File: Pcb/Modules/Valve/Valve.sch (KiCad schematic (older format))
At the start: 19 parts, among them CON1 Valve1, CON2 Valve3, CON3 Power, CON4 Valve2, CON5 Valve4, J1 JACK_RJ45, P1 Servo1, P2 Servo2, Q1 Q_NMOS_GSD, Q2 Q_NMOS_GSD, Q3 Q_NMOS_GSD, Q4 Q_NMOS_GSD

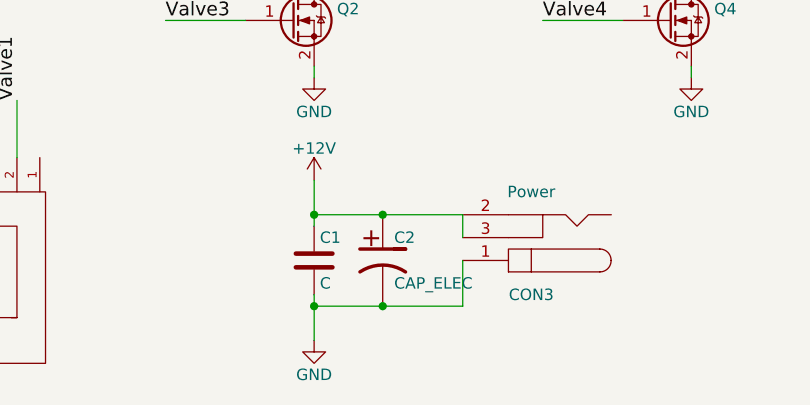
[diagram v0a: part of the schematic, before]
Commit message: Update module pcbs to common format and fix issues.
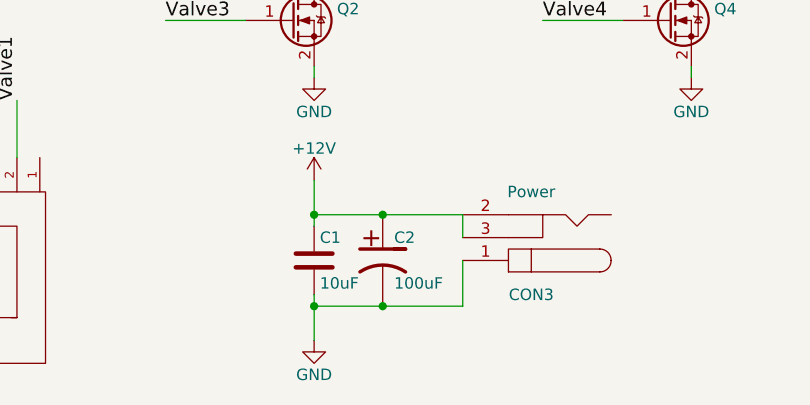
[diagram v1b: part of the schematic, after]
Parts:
- C1: value C -> 10uF
- C2: value CAP_ELEC -> 100uF
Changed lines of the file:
@@
 LIBS:valves
 LIBS:CA6
+LIBS:Valve-cache
 EELAYER 25 0
 EELAYER END
@@
 P 3800 3950
 F 0 "C2" H 3850 4050 50  0000 L CNN
-F 1 "CAP_ELEC" H 3850 3850 50  0000 L CNN
+F 1 "100uF" H 3850 3850 50  0000 L CNN
 F 2 "CA6:c_elec_6.3x5.7" H 3800 3950 60  0001 C CNN
 F 3 "" H 3800 3950 60  0000 C CNN
@@
 P 3500 3950
 F 0 "C1" H 3525 4050 50  0000 L CNN
-F 1 "C" H 3525 3850 50  0000 L CNN
+F 1 "10uF" H 3525 3850 50  0000 L CNN
 F 2 "Capacitors_SMD:C_1206" H 3538 3800 50  0001 C CNN
 F 3 "" H 3500 3950 50  0000 C CNN

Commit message: Update Valve module
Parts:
- added D5: LED, LEDs:LED_0805, symbol LED
- added R1, R3, R5, R7, R9: 1K, Resistors_SMD:R_0603, symbol R
- added R2, R4, R6, R8: 10K, Resistors_SMD:R_0603, symbol R
- added X1, X2, X3, X4: HOLE, Mounting_Holes:MountingHole_2.2mm_M2_ISO14580_Pad, symbol HOLE
- renumbered CON3 to POWER1, Q3 to Q2, Q2 to Q3, CON1 to Valve1, CON4 to Valve2, CON2 to Valve3, CON5 to Valve4
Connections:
- net +12V: now also POWER1.1, Valve1.1, Valve2.1, Valve3.1, Valve4.1, R9.1; no longer POWER1.2, POWER1.3, Valve1.2, Valve1.3, Valve2.2, Valve2.3, Valve3.2, Valve3.3, Valve4.2, Valve4.3
- net GND: now also POWER1.2, D5.1 (K), R2.1, R4.1, R6.1, R8.1; no longer POWER1.1
- net Valve1: now also R1.2; no longer Q1.1 (G)
- net Valve2: now also R3.2; no longer Q2.1 (G)
- net Valve3: now also R5.2; no longer Q3.1 (G)
- net Valve4: now also R7.2; no longer Q4.1 (G)
- net at D1.2 (A), Q1.3 (D): now also Valve1.2; no longer Valve1.1
- net at D3.2 (A), Q2.3 (D): now also Valve2.2; no longer Valve2.1
- net at D2.2 (A), Q3.3 (D): now also Valve3.2; no longer Valve3.1
- net at D4.2 (A), Q4.3 (D): now also Valve4.2; no longer Valve4.1
- new net: Q1.1 (G), R1.1, R2.2
- new net: Q2.1 (G), R3.1, R4.2
- new net: Q3.1 (G), R5.1, R6.2
- new net: Q4.1 (G), R7.1, R8.2
- new net: D5.2 (A), R9.2
- no-connect marks 0 -> 6
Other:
- moved on the sheet: C1, C2, D2, D4, POWER1, Q3, Q4, Valve3, Valve4

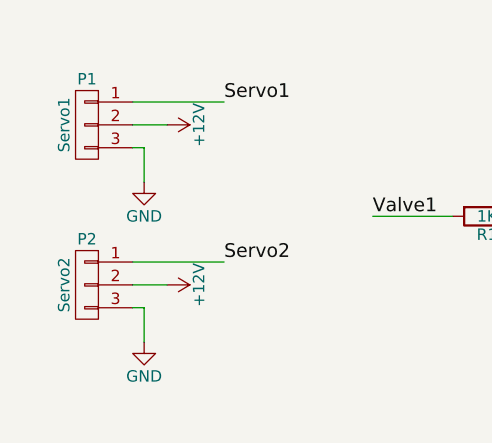
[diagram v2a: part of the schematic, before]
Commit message: Fix up PCB traces
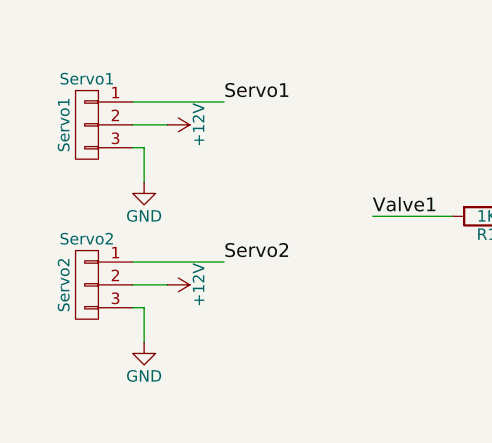
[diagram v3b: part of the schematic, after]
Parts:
- renumbered P1 to Servo1, P2 to Servo2
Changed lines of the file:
@@
 $EndComp
 $Comp
-L CONN_01X03 P1
+L CONN_01X03 Servo1
 U 1 1 59C16AB4
 P 1200 1150
-F 0 "P1" H 1200 1350 50  0000 C CNN
+F 0 "Servo1" H 1200 1350 50  0000 C CNN
 F 1 "Servo1" V 1300 1150 50  0000 C CNN
 F 2 "Socket_Strips:Socket_Strip_Angled_1x03_Pitch2.54mm" H 1200 1150 50  0001 C CNN
@@
 Servo1
 $Comp
-L CONN_01X03 P2
+L CONN_01X03 Servo2
 U 1 1 59C1A1B4
 P 1200 1850
-F 0 "P2" H 1200 2050 50  0000 C CNN
+F 0 "Servo2" H 1200 2050 50  0000 C CNN
 F 1 "Servo2" V 1300 1850 50  0000 C CNN
 F 2 "Socket_Strips:Socket_Strip_Angled_1x03_Pitch2.54mm" H 1200 1850 50  0001 C CNN

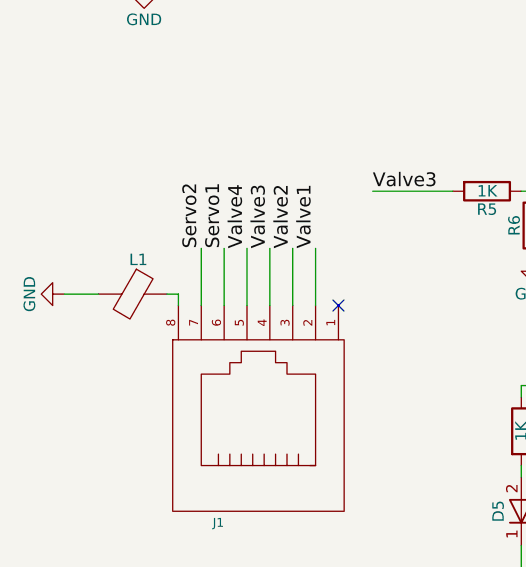
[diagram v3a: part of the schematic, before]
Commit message: Update module pcbs
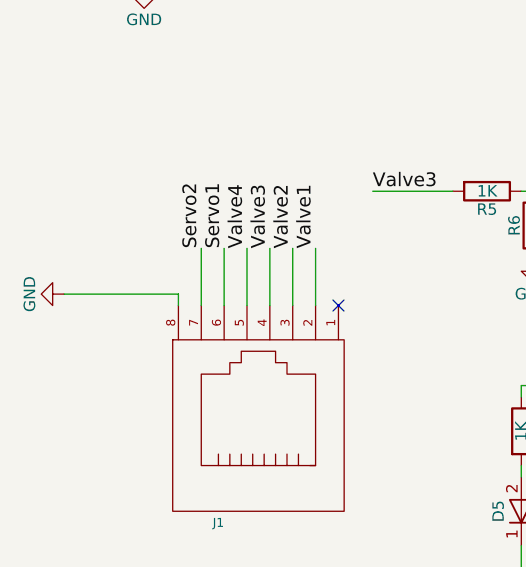
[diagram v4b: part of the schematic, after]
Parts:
- removed L1: Ferrite_Bead, Resistors_SMD:R_0805, symbol Ferrite_Bead
- X1, X2, X3, X4: footprint Mounting_Holes:MountingHole_2.2mm_M2_ISO14580_Pad -> Mounting_Holes:MountingHole_2.5mm_Pad
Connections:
- net GND: now also J1.8
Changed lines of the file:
@@
-$EndComp
-$Comp
-L Ferrite_Bead L1
-U 1 1 59C16933
-P 1400 3450
-F 0 "L1" V 1250 3475 50  0000 C CNN
-F 1 "Ferrite_Bead" V 1550 3450 50  0001 C CNN
-F 2 "Resistors_SMD:R_0805" V 1330 3450 50  0001 C CNN
-F 3 "" H 1400 3450 50  0000 C CNN
-	1    1400 3450
-	0    1    1    0
 $EndComp
 $Comp
@@
 $EndComp
 Wire Wire Line
-	1600 3500 1600 3450
-Wire Wire Line
-	1600 3450 1550 3450
+	1600 3450 1600 3500
+Wire Wire Line
+	1100 3450 1600 3450
 Wire Wire Line
 	2200 3500 2200 3250
@@
 $EndComp
 Wire Wire Line
-	1250 3450 1100 3450
-Wire Wire Line
 	1400 1250 1450 1250
 Wire Wire Line
@@
 F 0 "X1" H 6450 1050 60  0000 C CNN
 F 1 "HOLE" H 6450 1250 60  0000 C CNN
-F 2 "Mounting_Holes:MountingHole_2.2mm_M2_ISO14580_Pad" H 6450 1150 60  0001 C CNN
+F 2 "Mounting_Holes:MountingHole_2.5mm_Pad" H 6450 1150 60  0001 C CNN
 F 3 "" H 6450 1150 60  0000 C CNN
 	1    6450 1150
@@
 F 0 "X2" H 6450 1400 60  0000 C CNN
 F 1 "HOLE" H 6450 1600 60  0000 C CNN
-F 2 "Mounting_Holes:MountingHole_2.2mm_M2_ISO14580_Pad" H 6450 1500 60  0001 C CNN
+F 2 "Mounting_Holes:MountingHole_2.5mm_Pad" H 6450 1500 60  0001 C CNN
 F 3 "" H 6450 1500 60  0000 C CNN
 	1    6450 1500
@@
 F 0 "X3" H 6450 1750 60  0000 C CNN
 F 1 "HOLE" H 6450 1950 60  0000 C CNN
-F 2 "Mounting_Holes:MountingHole_2.2mm_M2_ISO14580_Pad" H 6450 1850 60  0001 C CNN
+F 2 "Mounting_Holes:MountingHole_2.5mm_Pad" H 6450 1850 60  0001 C CNN
 F 3 "" H 6450 1850 60  0000 C CNN
 	1    6450 1850
@@
 F 0 "X4" H 6450 2100 60  0000 C CNN
 F 1 "HOLE" H 6450 2300 60  0000 C CNN
-F 2 "Mounting_Holes:MountingHole_2.2mm_M2_ISO14580_Pad" H 6450 2200 60  0001 C CNN
+F 2 "Mounting_Holes:MountingHole_2.5mm_Pad" H 6450 2200 60  0001 C CNN
 F 3 "" H 6450 2200 60  0000 C CNN
 	1    6450 2200

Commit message: Update pcb for new switch
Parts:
- C1: symbol C -> Device:C
- C2: symbol CAP_ELEC -> CA6:CAP_ELEC
- D1, D2, D3, D4: symbol D -> Device:D
- D5: symbol LED -> Device:LED
- J1: symbol JACK_RJ45 -> CA6:JACK_RJ45
- POWER1, Valve1, Valve2, Valve3, Valve4: symbol BARREL_JACK -> Valve-rescue:BARREL_JACK
- Q1, Q2, Q3, Q4: symbol Q_NMOS_GSD -> Device:Q_NMOS_GSD
- R1, R2, R3, R4, R5, R6, R7, R8, R9: symbol R -> Device:R
- Servo1, Servo2: symbol CONN_01X03 -> Valve-rescue:CONN_01X03
- X1, X2, X3, X4: symbol HOLE -> CA6:HOLE
